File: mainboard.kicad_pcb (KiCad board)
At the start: 2 copper layers, 36 parts, among them J1 To battery holder, J2 To RED display, J3 To GREEN display, J4 To BLUE display, Q1 PNP S8550, Q2 NPN 2N5551, SW1 GREEN, SW2 STOP, SW3 START, SW4 RED, SW5 BLUE, U1 LM555xN, U2 CD4015 for RED, U3 CD4015 for GREEN, U4 CD4015 for BLUE

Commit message: first pcb version
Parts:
- added C6: 1uF, Capacitor_THT:CP_Radial_D4.0mm_P1.50mm, F.Cu at (237.5, 85.1)
- added H1: Frame, MountingHole:MountingHole_3.2mm_M3_DIN965_Pad, F.Cu at (162.6, 78.7)
- added H2: Frame, MountingHole:MountingHole_3.2mm_M3_DIN965_Pad, F.Cu at (246.4, 78.7)
- added H3: Frame, MountingHole:MountingHole_3.2mm_M3_DIN965_Pad, F.Cu at (246.4, 144.8)
- added H4: Frame, MountingHole:MountingHole_3.2mm_M3_DIN965_Pad, F.Cu at (162.6, 144.8)
- added H5: Battery holder, MountingHole:MountingHole_3.2mm_M3_DIN965_Pad, F.Cu at (170.2, 109.2)
- added H6: Battery holder, MountingHole:MountingHole_3.2mm_M3_DIN965_Pad, F.Cu at (215.9, 109.2)
- moved J4 202.1 mm to (224.8, 71.1), turned to 90 degrees
- moved R3 188.8 mm to (228.6, 86.4), turned to 270 degrees
- moved SW5 179.9 mm to (228.6, 129.5), turned to 90 degrees
- moved U3 174.1 mm to (199.4, 80.0)
- moved R4 165.6 mm to (241.3, 96.5), turned to 90 degrees
- moved R13 159.9 mm to (236.2, 109.2), turned to 180 degrees
- moved R2 157.8 mm to (226.1, 96.5), turned to 90 degrees
- moved U4 155.3 mm to (213.4, 80.0)
- moved SW4 154.4 mm to (200.7, 129.5), turned to 90 degrees
- moved C1 154.1 mm to (233.7, 86.4), turned to 180 degrees
- moved R12 150.9 mm to (226.1, 111.8)
- moved U2 148.9 mm to (185.4, 80.0)
- moved U1 147.9 mm to (238.8, 96.5), turned to 180 degrees
- moved SW2 146.1 mm to (193.0, 139.7)
- moved J3 145.5 mm to (193.0, 71.1), turned to 90 degrees
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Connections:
- Q1 pad 1: Net-(Q1-Pad1) -> VCC_MAIN
- Q1 pad 3: VCC_MAIN -> Net-(Q1-Pad3)
- Q2 pad 1: Net-(Q2-Pad1) -> GND_MAIN
- Q2 pad 2: GND_MAIN -> Net-(Q2-Pad2)
- R5 pad 1: Net-(Q1-Pad1) -> Net-(Q1-Pad2)
- R6 pad 2: Net-(Q1-Pad1) -> Net-(Q1-Pad2)
- R7 pad 1: Net-(Q2-Pad1) -> Net-(Q2-Pad2)
- R7 pad 2: Net-(Q1-Pad2) -> Net-(Q1-Pad3)
- SW2 pad 1: Net-(Q2-Pad1) -> Net-(Q2-Pad2)
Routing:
- net GND_MAIN: track 0.00 -> 400.4 mm
- net VCC_MAIN: track 0.00 -> 345.8 mm
- net CLOCK: track 0.00 -> 115.1 mm
- net GND: track 0.00 -> 110.2 mm
- net /red4: track 0.00 -> 74.3 mm
- net Net-(Q2-Pad2): track 0.00 -> 71.8 mm
- net GREEN: track 0.00 -> 65.2 mm
- net /grn4: track 0.00 -> 52.7 mm
- net BLUE: track 0.00 -> 51.0 mm
- net RED: track 0.00 -> 50.1 mm
- net /blu8: track 0.00 -> 39.2 mm
- net /red5: track 0.00 -> 37.2 mm
- net /red6: track 0.00 -> 37.2 mm
- net /red7: track 0.00 -> 36.4 mm
- net /blu3: track 0.00 -> 32.0 mm
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- added copper zone on B.Cu, net GND_MAIN
- added copper zone on F.Cu, net GND_MAIN
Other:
- board outline added: 94 x 88.9 mm
- net class Power added: clearance 0.2, trace_width 1.25, via_dia 2.9, via_drill 0.4

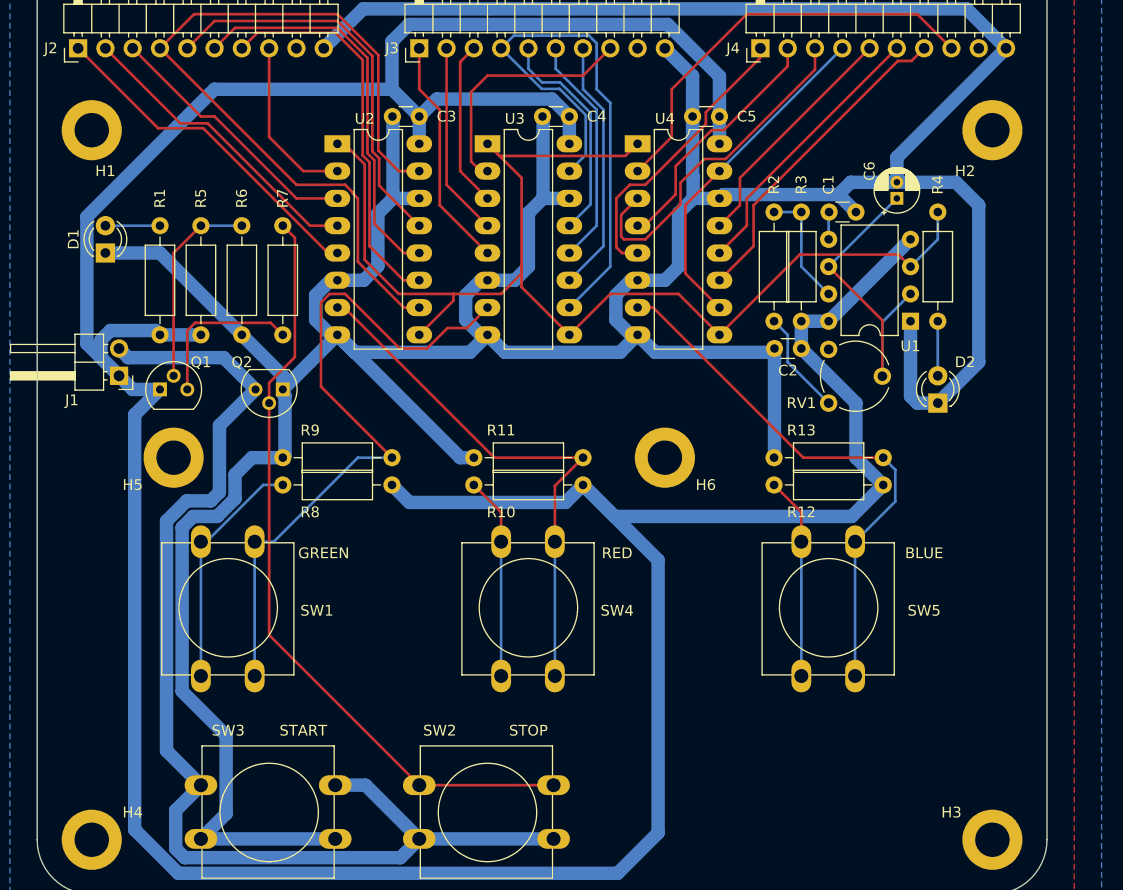
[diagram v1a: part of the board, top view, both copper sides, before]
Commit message: update silkscreen, gallery
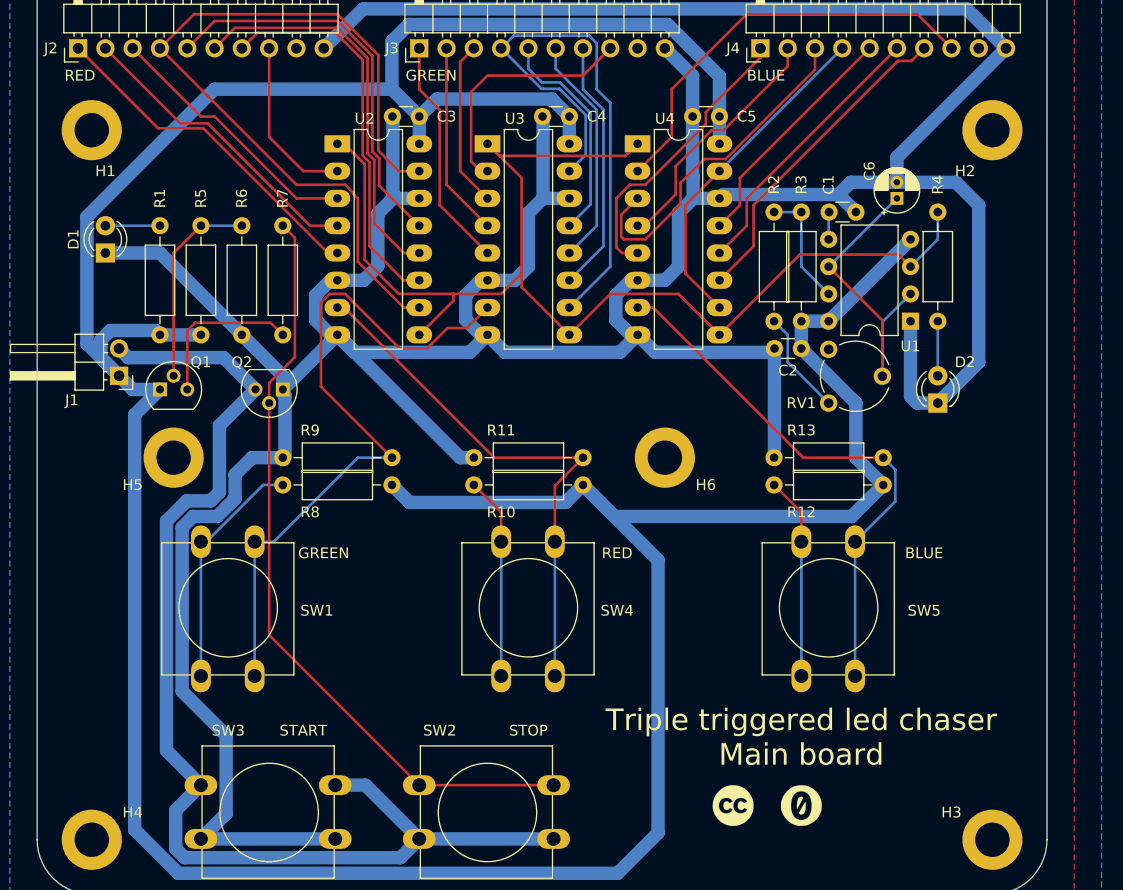
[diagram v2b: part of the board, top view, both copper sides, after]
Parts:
- added G***: LOGO, cliparts:logo--cc--zero, F.Cu at (228.6, 141.6)
- added G***: LOGO, cliparts:logo--cc--cc, F.Cu at (222.2, 141.6)
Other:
- board text added: "BLUE"
- board text added: "GREEN"
- board text added: "RED"
- board text added: "Triple triggered led chaser Main board"
